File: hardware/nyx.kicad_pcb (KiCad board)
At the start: 2 copper layers, 15 parts, among them J2 USB_C, U2 74LVC1G18, U3 USBLC6-2SC6, U5 TPS22919, U6 TPS22919, U7 INA226, U8 STM32F411CEUx, X2 12MHz

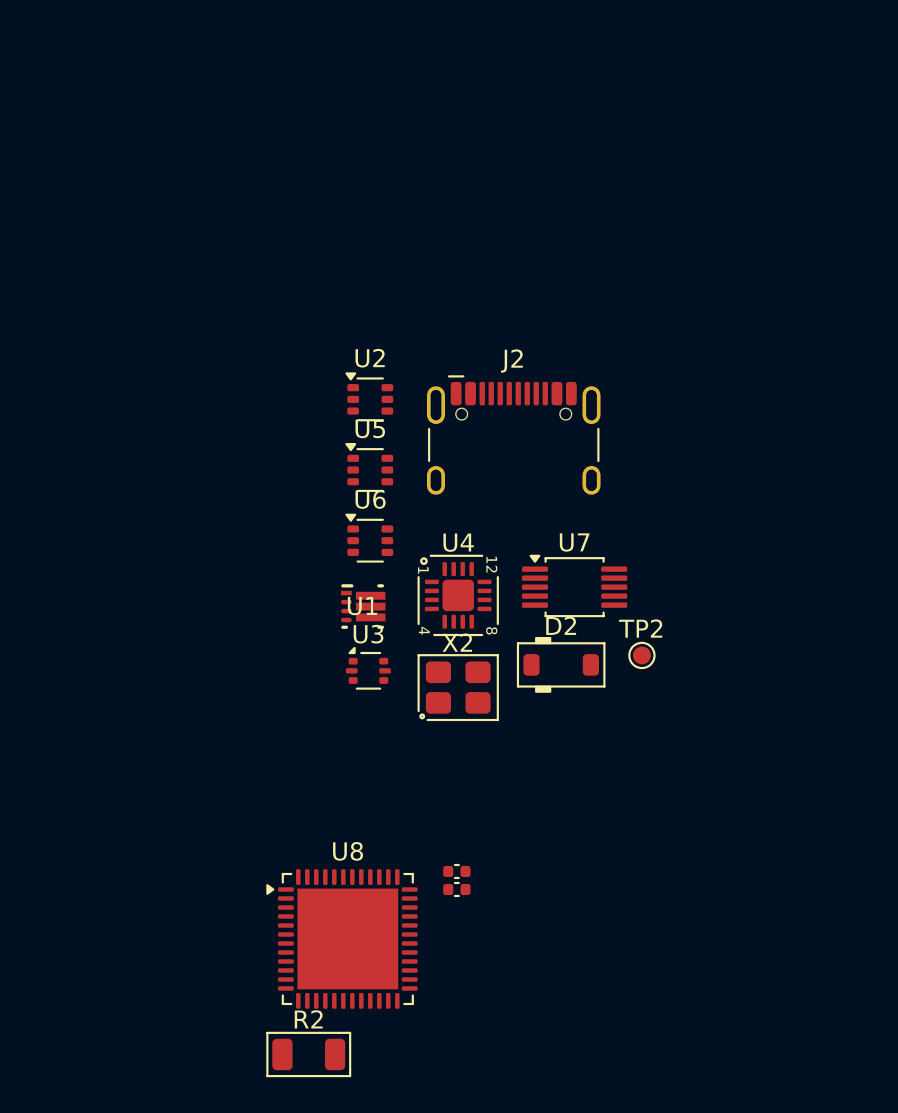
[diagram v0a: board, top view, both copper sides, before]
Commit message: ✨ Complete footprint assignment
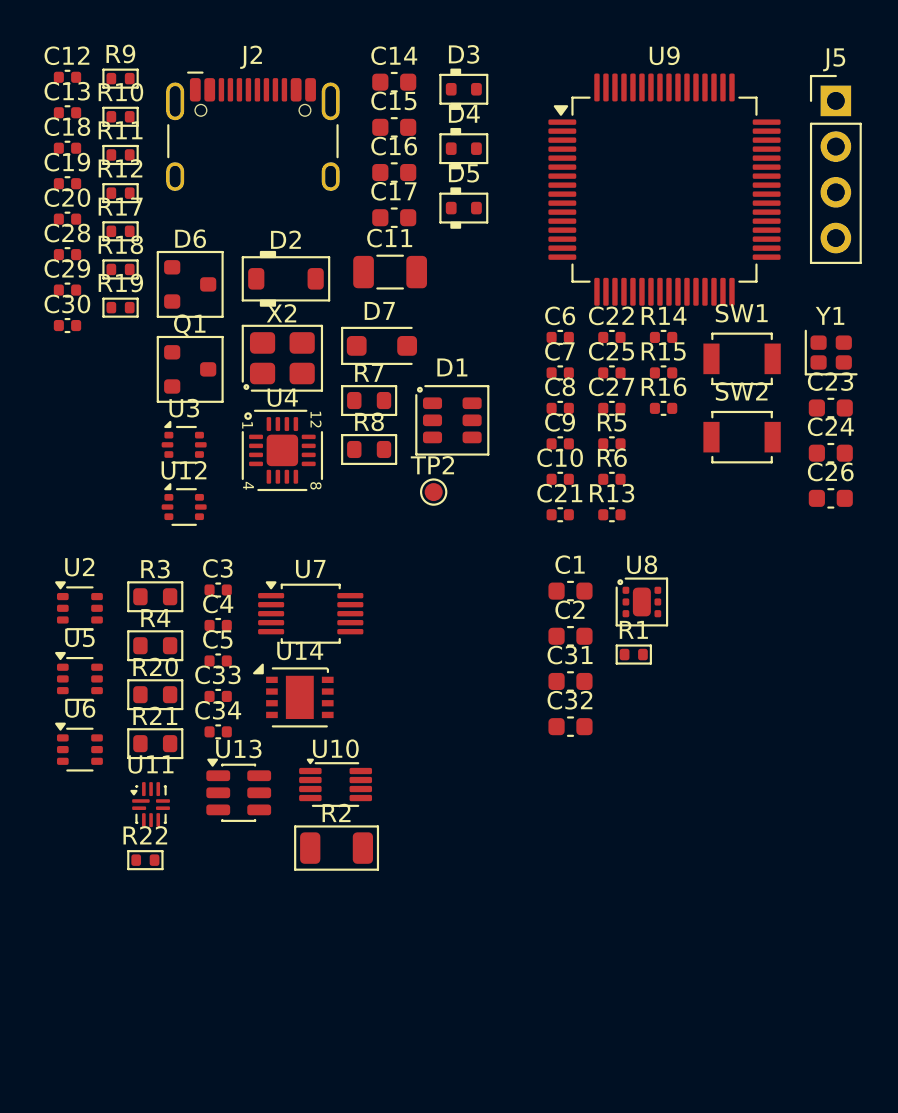
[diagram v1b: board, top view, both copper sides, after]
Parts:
- removed U1: ~, Package_SON:RLT0007A
- added C1: 10uF, Capacitor_SMD:C_0603_1608Metric, F.Cu at (142.6, 87.7)
- added C10: 100nF, Capacitor_SMD:C_0402_1005Metric, F.Cu at (142.1, 81.5)
- added C11: 4.7nF/2kV, Capacitor_SMD:C_1206_3216Metric, F.Cu at (132.6, 70.0)
- added C12: 10nF, Capacitor_SMD:C_0402_1005Metric, F.Cu at (114.7, 59.2)
- added C13: 100nF, Capacitor_SMD:C_0402_1005Metric, F.Cu at (114.7, 61.2)
- added C14: 4.7uF, Capacitor_SMD:C_0603_1608Metric, F.Cu at (132.8, 59.5)
- added C15: 4.7uF, Capacitor_SMD:C_0603_1608Metric, F.Cu at (132.8, 62.0)
- added C16: 10uF, Capacitor_SMD:C_0603_1608Metric, F.Cu at (132.8, 64.5)
- added C17: 1uF, Capacitor_SMD:C_0603_1608Metric, F.Cu at (132.8, 67.0)
- added C18: 100nF, Capacitor_SMD:C_0402_1005Metric, F.Cu at (114.7, 63.1)
- added C2: 22uF, Capacitor_SMD:C_0603_1608Metric, F.Cu at (142.6, 90.2)
- added C21: 12pF, Capacitor_SMD:C_0402_1005Metric, F.Cu at (142.1, 83.5)
- added C22: 12pF, Capacitor_SMD:C_0402_1005Metric, F.Cu at (144.9, 73.6)
- added C23: 2.2uF, Capacitor_SMD:C_0603_1608Metric, F.Cu at (157.1, 77.6)
- added C24: 2.2uF, Capacitor_SMD:C_0603_1608Metric, F.Cu at (157.1, 80.1)
- added C25: 100nF, Capacitor_SMD:C_0402_1005Metric, F.Cu at (144.9, 75.6)
- added C26: 4.7uF, Capacitor_SMD:C_0603_1608Metric, F.Cu at (157.1, 82.6)
- added C27: 100nF, Capacitor_SMD:C_0402_1005Metric, F.Cu at (144.9, 77.6)
- added C28: 100nF, Capacitor_SMD:C_0402_1005Metric, F.Cu at (114.7, 69.0)
- added C29: 100nF, Capacitor_SMD:C_0402_1005Metric, F.Cu at (114.7, 71.0)
- added C3: 100nF, Capacitor_SMD:C_0402_1005Metric, F.Cu at (123.1, 87.7)
- added C30: 100nF, Capacitor_SMD:C_0402_1005Metric, F.Cu at (114.7, 73.0)
- added C31: 2.2uF, Capacitor_SMD:C_0603_1608Metric, F.Cu at (142.6, 92.7)
- added C32: 1uF, Capacitor_SMD:C_0603_1608Metric, F.Cu at (142.6, 95.3)
- added C33: 100nF, Capacitor_SMD:C_0402_1005Metric, F.Cu at (123.1, 93.6)
- added C34: 100nF, Capacitor_SMD:C_0402_1005Metric, F.Cu at (123.1, 95.5)
- added C4: 100nF, Capacitor_SMD:C_0402_1005Metric, F.Cu at (123.1, 89.6)
- added C5: 100nF, Capacitor_SMD:C_0402_1005Metric, F.Cu at (123.1, 91.6)
- added C6: 100nF, Capacitor_SMD:C_0402_1005Metric, F.Cu at (142.1, 73.6)
- added C7: 100nF, Capacitor_SMD:C_0402_1005Metric, F.Cu at (142.1, 75.6)
- added C8: 100nF, Capacitor_SMD:C_0402_1005Metric, F.Cu at (142.1, 77.6)
- added C9: 100nF, Capacitor_SMD:C_0402_1005Metric, F.Cu at (142.1, 79.5)
- added D1: SRV05-4, PCM_Package_TO_SOT_SMD_AKL:SOT-23-6, F.Cu at (136.1, 78.2)
- added D3: ESD5Z5V0, PCM_Diode_SMD_AKL:D_SOD-523, F.Cu at (136.7, 59.9)
- added D4: ESD5Z5V0, PCM_Diode_SMD_AKL:D_SOD-523, F.Cu at (136.7, 63.1)
- added D5: ESD5Z5V0, PCM_Diode_SMD_AKL:D_SOD-523, F.Cu at (136.7, 66.5)
- added D6: PESD2CAN, PCM_Package_TO_SOT_SMD_AKL:SOT-23, F.Cu at (121.5, 70.7)
- added D7: SMF5.0A, Diode_SMD:D_SOD-123F, F.Cu at (132.2, 74.1)
- added J5: Conn_MCU_PROG, Connector_PinHeader_2.54mm:PinHeader_1x04_P2.54mm_Vertical, F.Cu at (157.4, 60.5)
- added Q1: BSS123, PCM_Package_TO_SOT_SMD_AKL:SOT-23, F.Cu at (121.5, 75.4)
- added R1: 1M, PCM_Resistor_SMD_AKL:R_0402_1005Metric, F.Cu at (146.1, 91.2)
- added R10: 5.1k, PCM_Resistor_SMD_AKL:R_0402_1005Metric, F.Cu at (117.6, 61.4)
- added R11: 0, PCM_Resistor_SMD_AKL:R_0402_1005Metric, F.Cu at (117.6, 63.5)
- added R12: 0, PCM_Resistor_SMD_AKL:R_0402_1005Metric, F.Cu at (117.6, 65.6)
- added R13: 10k, Capacitor_SMD:C_0402_1005Metric, F.Cu at (144.9, 83.5)
- added R14: 10k, Capacitor_SMD:C_0402_1005Metric, F.Cu at (147.8, 73.6)
- added R15: 22, Capacitor_SMD:C_0402_1005Metric, F.Cu at (147.8, 75.6)
- added R16: 22, Capacitor_SMD:C_0402_1005Metric, F.Cu at (147.8, 77.6)
- added R17: 100k, PCM_Resistor_SMD_AKL:R_0402_1005Metric, F.Cu at (117.6, 67.7)
- added R18: 1k, PCM_Resistor_SMD_AKL:R_0402_1005Metric, F.Cu at (117.6, 69.9)
- added R19: 100k, PCM_Resistor_SMD_AKL:R_0402_1005Metric, F.Cu at (117.6, 72.0)
- added R20: 1k, PCM_Resistor_SMD_AKL:R_0603_1608Metric, F.Cu at (119.6, 93.5)
- added R21: 120R, PCM_Resistor_SMD_AKL:R_0603_1608Metric, F.Cu at (119.6, 96.2)
- added R22: 100k, PCM_Resistor_SMD_AKL:R_0402_1005Metric, F.Cu at (119.0, 102.7)
- added R3: 10, PCM_Resistor_SMD_AKL:R_0603_1608Metric, F.Cu at (119.6, 88.0)
- added R4: 10, PCM_Resistor_SMD_AKL:R_0603_1608Metric, F.Cu at (119.6, 90.8)
- added R5: 4.7k, Capacitor_SMD:C_0402_1005Metric, F.Cu at (144.9, 79.5)
- added R6: 4.7k, Capacitor_SMD:C_0402_1005Metric, F.Cu at (144.9, 81.5)
- added R7: 0, PCM_Resistor_SMD_AKL:R_0603_1608Metric, F.Cu at (131.4, 77.1)
- added R8: 1M, PCM_Resistor_SMD_AKL:R_0603_1608Metric, F.Cu at (131.4, 79.9)
- added R9: 5.1k, PCM_Resistor_SMD_AKL:R_0402_1005Metric, F.Cu at (117.6, 59.3)
- added SW1: SW_Push, Button_Switch_SMD:SW_SPST_B3U-1000P, F.Cu at (152.2, 74.8)
- added SW2: SW_Push, Button_Switch_SMD:SW_SPST_B3U-1000P, F.Cu at (152.2, 79.2)
- added U10: SN74LVC2T45DCUR, Package_SO:VSSOP-8_2.3x2mm_P0.5mm, F.Cu at (129.6, 98.5)
- added U11: TS3USB30ERSWR, Package_DFN_QFN:UQFN-10_1.4x1.8mm_P0.4mm, F.Cu at (119.3, 99.6)
- added U12: USBLC6-2SC6, Package_TO_SOT_SMD:SOT-666, F.Cu at (121.2, 83.1)
- added U13: TS5A3159DBV, Package_TO_SOT_SMD:SOT-23-6, F.Cu at (124.2, 98.9)
- added U14: MCP2542FDxMF, Package_DFN_QFN:DFN-8-1EP_3x3mm_P0.65mm_EP1.55x2.4mm, F.Cu at (127.6, 93.6)
- added U9: STM32F405RGTx, Package_QFP:LQFP-64_10x10mm_P0.5mm, F.Cu at (147.9, 65.4)
- added Y1: 25MHz, Crystal:Crystal_SMD_2016-4Pin_2.0x1.6mm, F.Cu at (157.1, 74.5)
- U8: value STM32F411CEUx -> TLV76733DRVx; footprint Package_DFN_QFN:QFN-48-1EP_7x7mm_P0.5mm_EP5.6x5.6mm -> PCM_Package_SON_AKL:WSON-6-1EP_2x2mm_P0.65mm_EP1x1.6mm
- moved C19 43.9 mm to (114.7, 65.1)
- moved C20 43.1 mm to (114.7, 67.1)
- moved D2 26.3 mm to (126.8, 70.4)
- moved U8 24.8 mm to (146.6, 88.3)
- moved J2 22.2 mm to (125.0, 63.6)
- moved X2 20.7 mm to (126.6, 74.8)
- moved U2 19.9 mm to (115.4, 88.7)
- moved U5 19.9 mm to (115.4, 92.6)
- moved U6 19.9 mm to (115.4, 96.5)
- moved U3 16.2 mm to (121.2, 79.6)
- moved U7 14.7 mm to (128.2, 89.0)
- moved TP2 14.7 mm to (135.0, 82.2)
- moved U4 12.7 mm to (126.6, 79.9)
- moved R2 11.6 mm to (129.6, 102.0)
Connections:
- net /D+ renamed /Connection/D+
- net /D- renamed /Connection/D-
- net 3.3EN renamed /IO/3.3V_EN
- net 5EN renamed /IO/5V_EN
- net 5VBUS renamed /IO/5V_VBUS
- net VBUS_PRE renamed /IO/IN+
- U2 pad 1: VBUS_SW -> /VBUS_SW
- U2 pad 3: VBUS_EN -> /VBUS_EN
- U4 pad 10: USB_D1+ -> /USB_D1+
- U4 pad 11: USB_DM -> /Connection/USB_DN
- U4 pad 12: USB_DP -> /Connection/USB_DP
- U4 pad 7: USB_D2- -> /Connection/USB_D2-
- U4 pad 8: USB_D2+ -> /Connection/USB_D2+
- U4 pad 9: USB_D1- -> /USB_D1-
- U6 pad 1: 3.3VBUS -> /IO/3.3V_VBUS
- U7 pad 4: SDA -> /SDA
- U7 pad 5: SCL -> /SCL
- U8 pad 2: unconnected-(U8-PC13-Pad2) -> +3.3V
- U8 pad 3: unconnected-(U8-PC14-Pad3) -> GND
- U8 pad 4: unconnected-(U8-PC15-Pad4) -> +5V
- U8 pad 5: Net-(U8-PH0) -> GND
- U8 pad 6: Net-(U8-PH1) -> +5V
- U8 pad 7: RESET -> GND
